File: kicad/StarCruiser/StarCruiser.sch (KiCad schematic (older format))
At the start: 108 parts, among them Q10 2N4126, Q11 2N4124, Q12 2N4127, Q13 2N4124, Q14 2N4124, Q15 2N4126, Q16 2N4124, Q18 2N4124, Q19 2N4126, Q20 2N4124, Q21 2N4124, Q6 2N4124, Q7 2N4124, Q7 2N4134, Q8 2N4124, Q9 2N4124, U2 LM741, U3 LM566, U4 LM566, U5 LM741, U6H 002

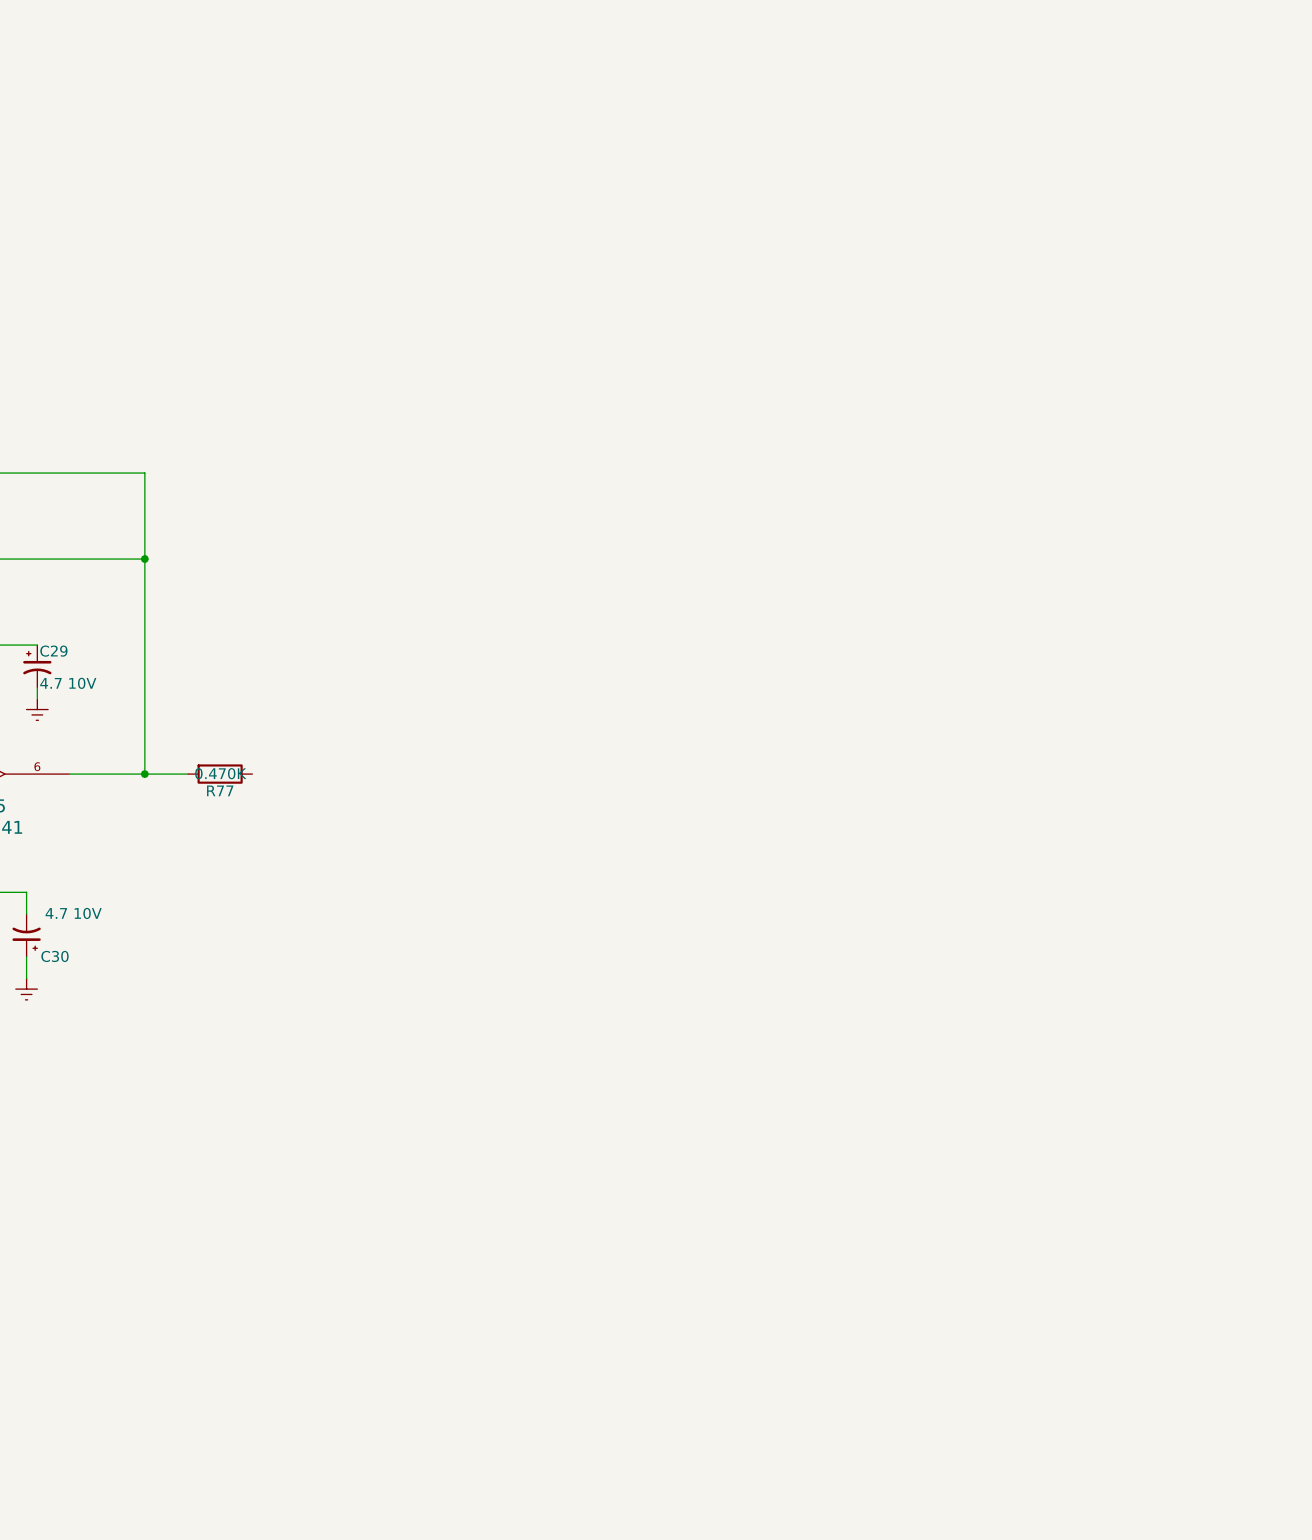
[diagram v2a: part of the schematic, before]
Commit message: Star Cruiser: finished schematics, this will need to be reviewed: there are some parts I can't read plus some components I don't recognize
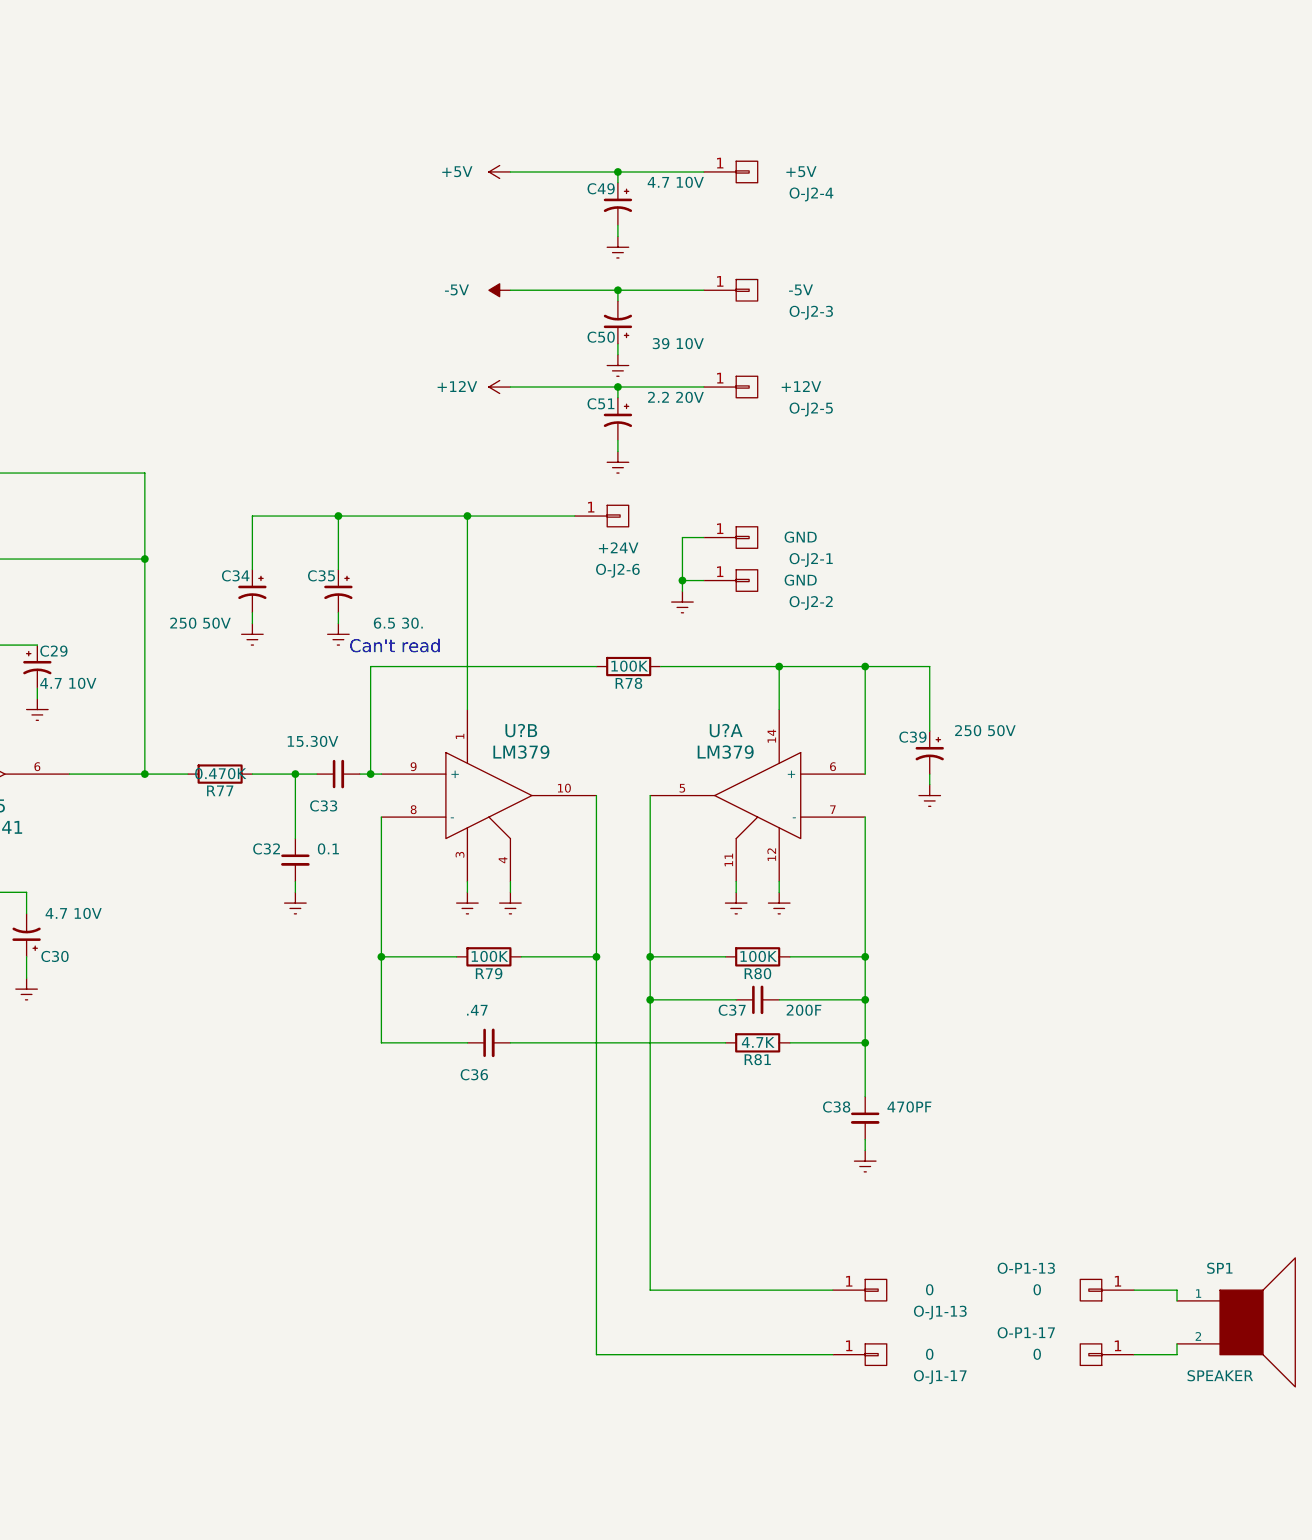
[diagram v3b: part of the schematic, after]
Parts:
- added C32: 0.1, symbol C_Small
- added C33: 15.30V, symbol C_Small
- added C34, C39: 250 50V, symbol CP1_Small
- added C35: 6.5 30., symbol CP1_Small
- added C36: .47, symbol C_Small
- added C37: 200F, symbol C_Small
- added C38: 470PF, symbol C_Small
- added C49: 4.7 10V, symbol CP1_Small
- added C50: 39 10V, symbol CP1_Small
- added C51: 2.2 20V, symbol CP1_Small
- added O-J1-13, O-J1-17, O-P1-13, O-P1-17: 0, symbol CONN_01X01
- added O-J2-1, O-J2-2: GND, symbol CONN_01X01
- added O-J2-3: -5V, symbol CONN_01X01
- added O-J2-4: +5V, symbol CONN_01X01
- added O-J2-5: +12V, symbol CONN_01X01
- added O-J2-6: +24V, symbol CONN_01X01
- added R78, R79, R80: 100K, symbol R
- added R81: 4.7K, symbol R
- added SP1: SPEAKER, symbol SPEAKER
- added U? (x2): LM379, symbol LM379
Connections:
- net +12V: now also C51.1, O-J2-5.1 (P1)
- net +5V: now also C49.1, O-J2-4.1 (P1)
- net -5V: now also C50.2, O-J2-3.1 (P1)
- net Earth: now also C32.2, C34.2, C35.2, C38.2, C39.2, C49.2, C50.1, C51.2, O-J2-1.1 (P1), O-J2-2.1 (P1), U?.11, U?.12, U?.3, U?.4
- net at R77.1: now also C32.1, C33.1
- new net: C39.1, R78.1, U?.14, U?.6 (+)
- new net: C37.1, O-J1-13.1 (P1), R80.2, U?.5
- new net: C37.2, C38.1, R80.1, R81.1, U?.7 (-)
- new net: C34.1, C35.1, O-J2-6.1 (P1), U?.1
- new net: O-J1-17.1 (P1), R79.1, U?.10
- new net: C36.1, R79.2, U?.8 (-)
- new net: C33.2, R78.2, U?.9 (+)
- new net: C36.2, R81.2
- new net: O-P1-13.1 (P1), SP1.1
- new net: O-P1-17.1 (P1), SP1.2
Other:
- note added: "Can't read"
